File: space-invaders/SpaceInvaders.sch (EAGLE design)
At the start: 26 parts, among them J2_J4 TM4C123GXL, J3_J1 TM4C123GXL, J5 Nokia 5110, J6 Nokia 5110, U1 5V Voltage Regulator

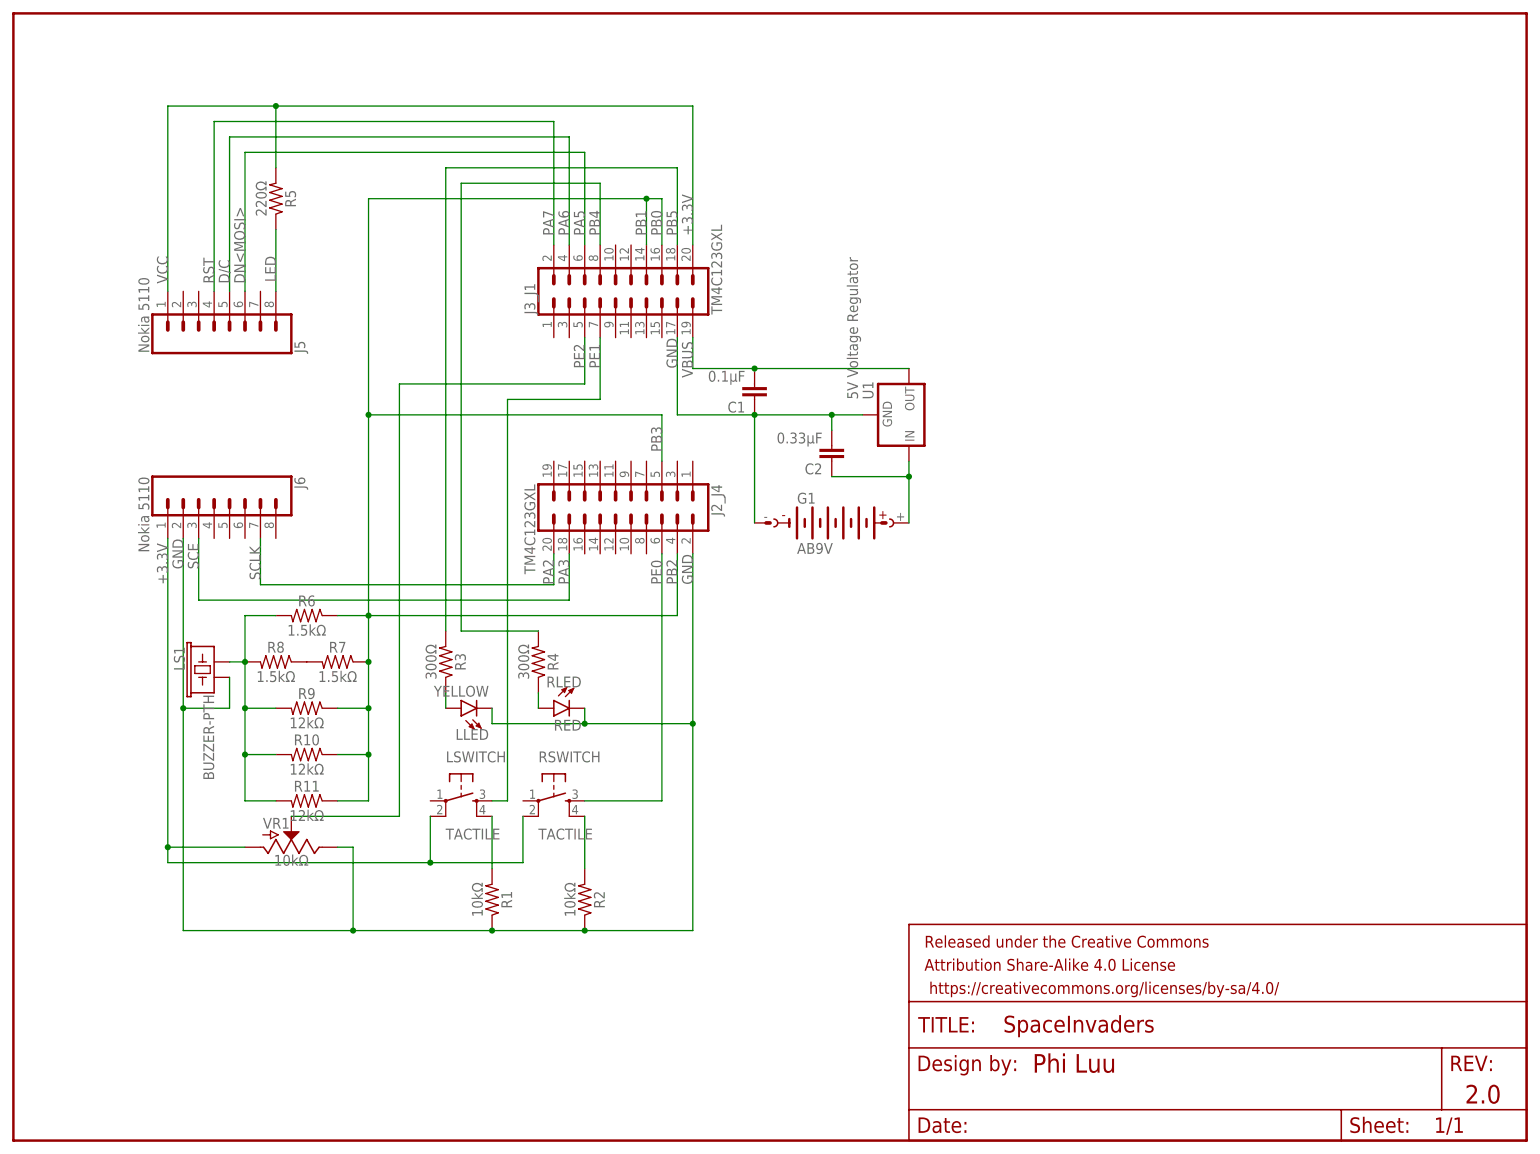
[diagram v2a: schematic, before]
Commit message: Setup SpaceInvaders regular manufacturing
Default EAGLE Design Rule Check (DRC). Double sided.
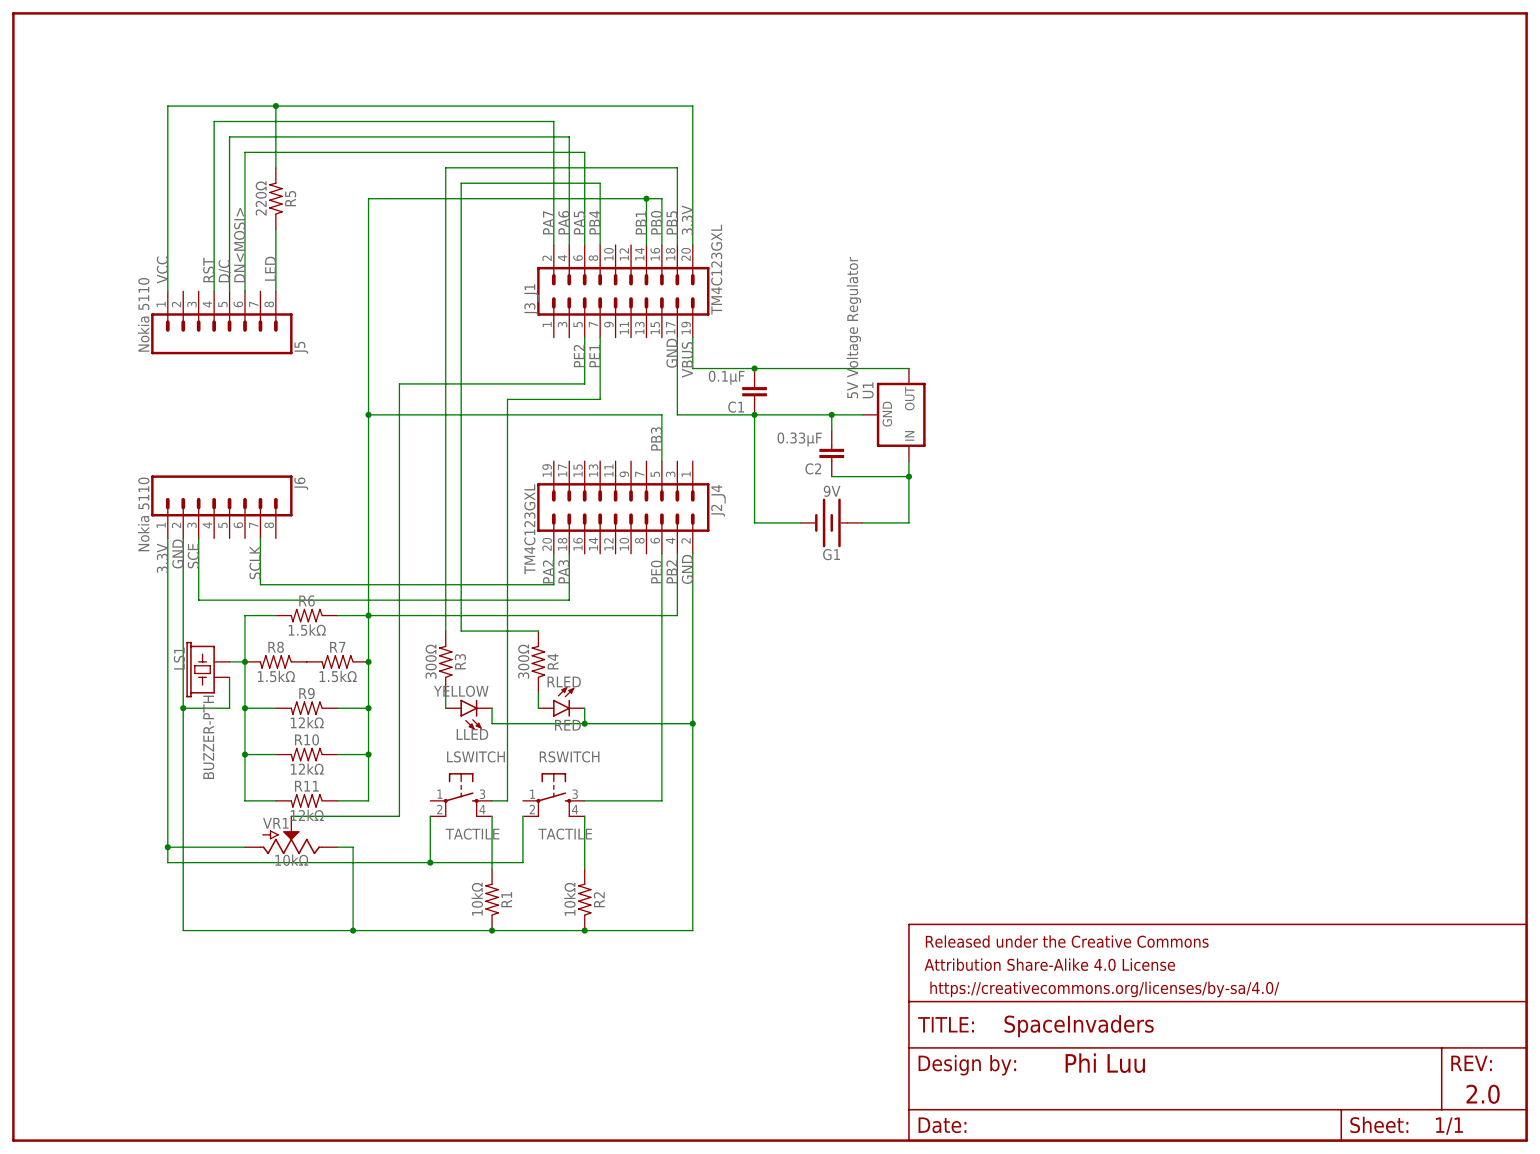
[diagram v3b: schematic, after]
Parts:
- G1: value AB9V -> 9V; device battery:AB9V -> SparkFun-Batteries:BATTERY-9V
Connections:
- net +3.3V renamed 3.3V
- net N$12 renamed LSWITCH_GND
- net N$14 renamed RSWITCH_GND
- net N$17 renamed RLED
- net N$19 renamed LLED
- net N$23 renamed DAC_OUT
- net N$24 renamed 9V
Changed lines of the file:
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@@
 <part name="C2" library="SparkFun-Capacitors" deviceset="0.1UF" device="-KIT-EZ-50V-20%" value="0.33μF"/>
 <part name="U1" library="SparkFun-IC-Power" deviceset="V_REG_78XX" device="-TO-220" value="5V Voltage Regulator"/>
-<part name="G1" library="battery" deviceset="AB9V" device=""/>
+<part name="G1" library="SparkFun-Batteries" deviceset="BATTERY" device="-9V" value="9V"/>
 <part name="FRAME1" library="SparkFun-Aesthetics" deviceset="FRAME-LETTER" device=""/>
 </parts>
@@
 <sheet>
 <plain>
-<text x="167.64" y="12.7" size="3.048" layer="94" font="vector" align="center-left">Phi Luu</text>
+<text x="172.72" y="12.7" size="3.048" layer="94" font="vector" align="center-left">Phi Luu</text>
 <text x="238.76" y="7.62" size="3.048" layer="94" font="vector" align="center-left">2.0</text>
 <text x="106.68" y="148.844" size="1.778" layer="96" font="vector" rot="R90">PB0</text>
@@
 <instance part="C2" gate="G$1" x="134.62" y="114.3" rot="R180"/>
 <instance part="U1" gate="G$1" x="147.32" y="119.38" rot="MR90"/>
-<instance part="G1" gate="G$1" x="134.62" y="101.6"/>
+<instance part="G1" gate="G$1" x="134.62" y="101.6" rot="R180"/>
 <instance part="FRAME1" gate="G$1" x="0" y="0"/>
 <instance part="FRAME1" gate="V" x="147.32" y="0"/>
@@
 </segment>
 </net>
-<net name="N$12" class="0">
+<net name="LSWITCH_GND" class="0">
 <segment>
 <pinref part="LSWITCH" gate="S" pin="4"/>
@@
 </segment>
 </net>
-<net name="N$14" class="0">
+<net name="RSWITCH_GND" class="0">
 <segment>
 <pinref part="RSWITCH" gate="S" pin="4"/>
@@
 </segment>
 </net>
-<net name="N$17" class="0">
+<net name="RLED" class="0">
 <segment>
 <pinref part="R4" gate="G$1" pin="1"/>
@@
 </segment>
 </net>
-<net name="N$19" class="0">
+<net name="LLED" class="0">
 <segment>
 <pinref part="R3" gate="G$1" pin="1"/>
@@
 </segment>
 </net>
-<net name="N$23" class="0">
+<net name="DAC_OUT" class="0">
 <segment>
 <pinref part="R6" gate="G$1" pin="2"/>
@@
 </segment>
 </net>
-<net name="N$24" class="0">
-<segment>
-<pinref part="G1" gate="G$1" pin="+"/>
+<net name="9V" class="0">
+<segment>
 <pinref part="U1" gate="G$1" pin="IN"/>
-<wire x1="147.32" y1="101.6" x2="147.32" y2="109.22" width="0.1524" layer="91"/>
 <pinref part="C2" gate="G$1" pin="1"/>
 <wire x1="147.32" y1="109.22" x2="147.32" y2="111.76" width="0.1524" layer="91"/>
 <wire x1="134.62" y1="109.22" x2="147.32" y2="109.22" width="0.1524" layer="91"/>
+<pinref part="G1" gate="G$1" pin="+"/>
+<wire x1="139.7" y1="101.6" x2="147.32" y2="101.6" width="0.1524" layer="91"/>
+<wire x1="147.32" y1="101.6" x2="147.32" y2="109.22" width="0.1524" layer="91"/>
 <junction x="147.32" y="109.22"/>
 </segment>
@@
 <wire x1="109.22" y1="119.38" x2="121.92" y2="119.38" width="0.1524" layer="91"/>
 <junction x="121.92" y="119.38"/>
-<pinref part="G1" gate="G$1" pin="-"/>
-<wire x1="121.92" y1="119.38" x2="121.92" y2="101.6" width="0.1524" layer="91"/>
 <pinref part="C2" gate="G$1" pin="2"/>
 <wire x1="134.62" y1="116.84" x2="134.62" y2="119.38" width="0.1524" layer="91"/>
 <junction x="134.62" y="119.38"/>
 <label x="109.22" y="127" size="1.778" layer="95" font="vector" rot="R90"/>
+<pinref part="G1" gate="G$1" pin="-"/>
+<wire x1="129.54" y1="101.6" x2="121.92" y2="101.6" width="0.1524" layer="91"/>
+<wire x1="121.92" y1="101.6" x2="121.92" y2="119.38" width="0.1524" layer="91"/>
 </segment>
 <segment>
@@
 </segment>
 </net>
-<net name="+3.3V" class="0">
+<net name="LED" class="0">
+<segment>
+<pinref part="R5" gate="G$1" pin="1"/>
+<pinref part="J5" gate="G$1" pin="8"/>
+<wire x1="43.18" y1="149.86" x2="43.18" y2="139.7" width="0.1524" layer="91"/>
+<label x="43.18" y="141.224" size="1.778" layer="95" font="vector" rot="R90"/>
+</segment>
+</net>
+<net name="PA3" class="0">
+<segment>
+<pinref part="J6" gate="G$1" pin="3"/>
+<wire x1="30.48" y1="99.06" x2="30.48" y2="88.9" width="0.1524" layer="91"/>
+<pinref part="J2_J4" gate="G$1" pin="18"/>
+<wire x1="30.48" y1="88.9" x2="91.44" y2="88.9" width="0.1524" layer="91"/>
+<wire x1="91.44" y1="88.9" x2="91.44" y2="96.52" width="0.1524" layer="91"/>
+<label x="91.44" y="91.44" size="1.778" layer="95" font="vector" rot="R90"/>
+</segment>
+</net>
+<net name="3.3V" class="0">
 <segment>
 <pinref part="J3_J1" gate="G$1" pin="20"/>
@@
 <wire x1="68.58" y1="53.34" x2="68.58" y2="45.72" width="0.1524" layer="91"/>
 <junction x="68.58" y="45.72"/>
-<label x="25.4" y="91.44" size="1.778" layer="95" font="vector" rot="R90"/>
-</segment>
-</net>
-<net name="LED" class="0">
-<segment>
-<pinref part="R5" gate="G$1" pin="1"/>
-<pinref part="J5" gate="G$1" pin="8"/>
-<wire x1="43.18" y1="149.86" x2="43.18" y2="139.7" width="0.1524" layer="91"/>
-<label x="43.18" y="141.224" size="1.778" layer="95" font="vector" rot="R90"/>
-</segment>
-</net>
-<net name="PA3" class="0">
-<segment>
-<pinref part="J6" gate="G$1" pin="3"/>
-<wire x1="30.48" y1="99.06" x2="30.48" y2="88.9" width="0.1524" layer="91"/>
-<pinref part="J2_J4" gate="G$1" pin="18"/>
-<wire x1="30.48" y1="88.9" x2="91.44" y2="88.9" width="0.1524" layer="91"/>
-<wire x1="91.44" y1="88.9" x2="91.44" y2="96.52" width="0.1524" layer="91"/>
-<label x="91.44" y="91.44" size="1.778" layer="95" font="vector" rot="R90"/>
+<label x="25.4" y="93.218" size="1.778" layer="95" font="vector" rot="R90"/>
 </segment>
 </net>
@@
 </sheet>
 </sheets>
+<errors>
+</errors>
 </schematic>
 </drawing>

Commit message: Update board SpaceInvaders
Add names to empty pins
Naming convention
Change switch package
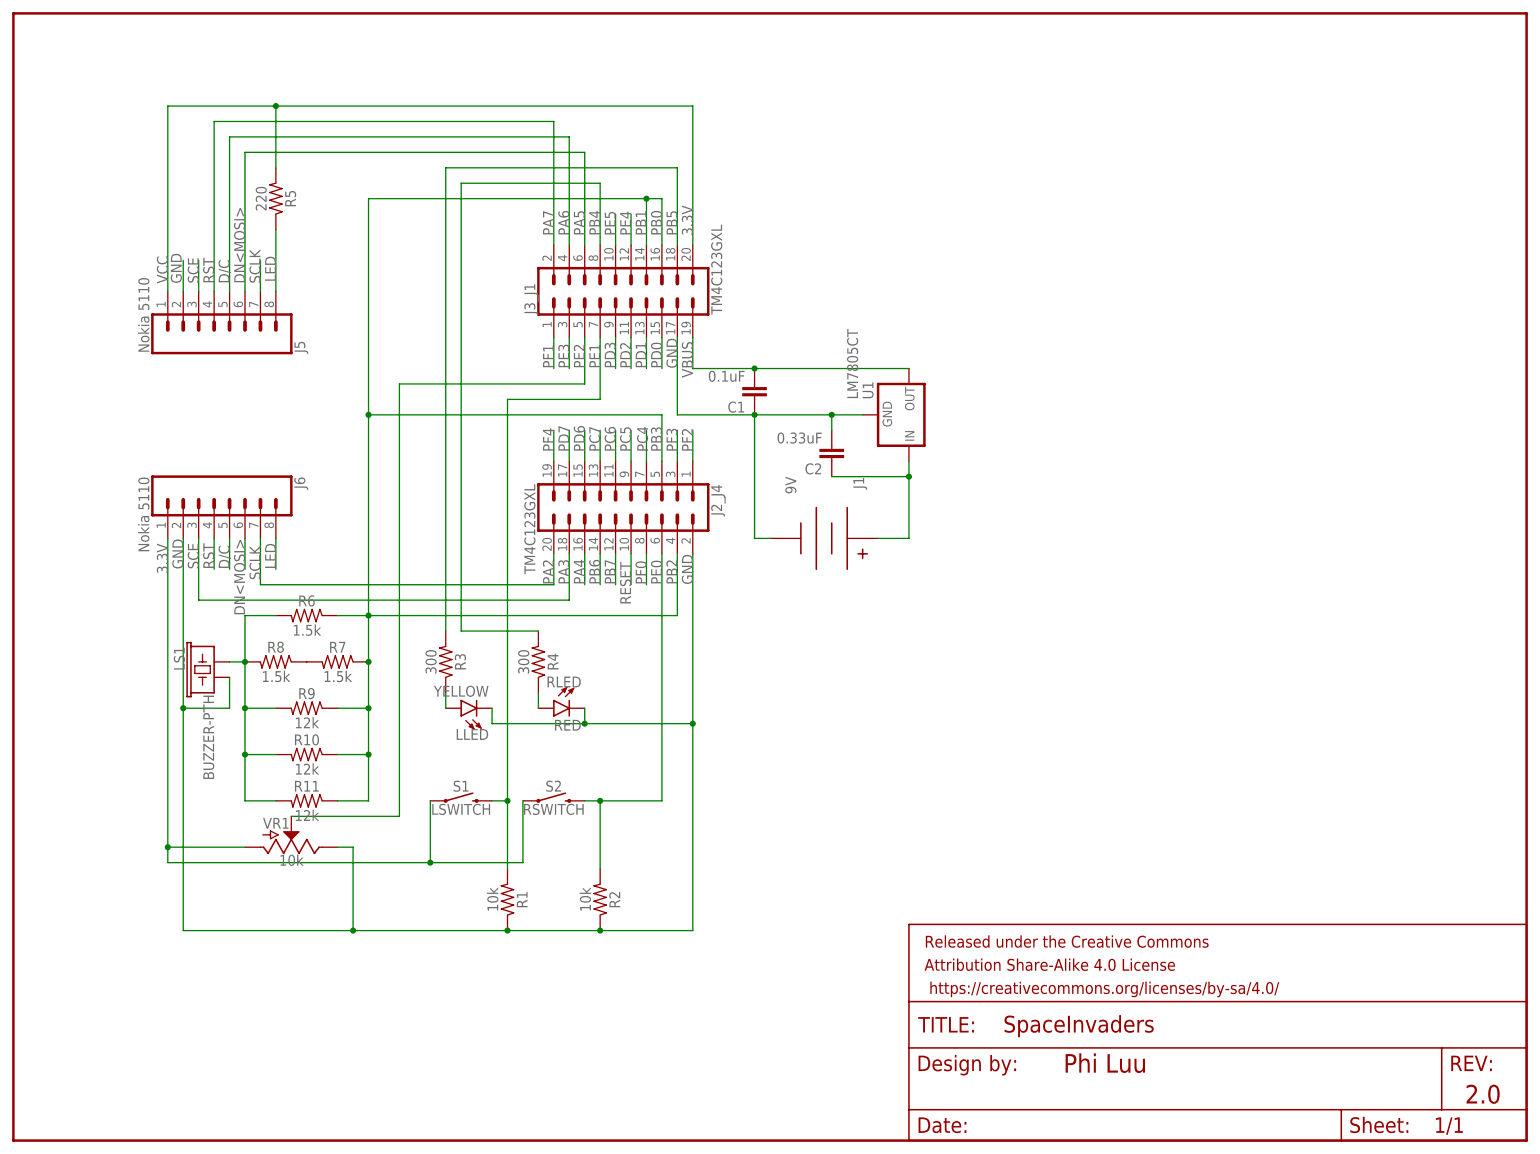
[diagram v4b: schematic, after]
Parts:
- removed G1: 9V, SparkFun-Batteries:BATTERY-9V
- removed LSWITCH, RSWITCH: TACTILE, SparkFun-Retired:TAC_SWITCHPTH
- added J1: 9V, SparkFun-Connectors:BC9VPC
- added S1: LSWITCH, SparkFun-Switches:MOMENTARY-SWITCH-SPST-PTH-6.0MM
- added S2: RSWITCH, SparkFun-Switches:MOMENTARY-SWITCH-SPST-PTH-6.0MM
- C1: value 0.1μF -> 0.1uF
- C2: value 0.33μF -> 0.33uF
- R1, R2, VR1: value 10kΩ -> 10k
- R10, R11, R9: value 12kΩ -> 12k
- R3, R4: value 300Ω -> 300
- R5: value 220Ω -> 220
- R6, R7, R8: value 1.5kΩ -> 1.5k
- U1: value 5V Voltage Regulator -> LM7805CT
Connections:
- removed net LSWITCH_GND: LSWITCH.4, R1.2
- removed net RSWITCH_GND: R2.2, RSWITCH.4
- new net D/C: J6.5
- new net DN<MOSI>: J6.6
- new net PA4: J2_J4.16
- new net PB6: J2_J4.14
- new net PB7: J2_J4.12
- new net PC4: J2_J4.7
- new net PC5: J2_J4.9
- new net PC6: J2_J4.11
- new net PC7: J2_J4.13
- new net PD0: J3_J1.15
- new net PD1: J3_J1.13
- new net PD2: J3_J1.11
- new net PD3: J3_J1.9
- new net PD6: J2_J4.15
- new net PD7: J2_J4.17
- new net PE3: J3_J1.3
- new net PE4: J3_J1.12
- new net PE5: J3_J1.10
- new net PF0: J2_J4.8
- new net PF1: J3_J1.1
- new net PF2: J2_J4.1
- new net PF3: J2_J4.3
- new net PF4: J2_J4.19
- new net RESET: J2_J4.10
- new net RST: J6.4
- new net SCE: J5.3
- new net SCLK: J5.7
- net 3.3V: now also S1.1, S2.1; no longer LSWITCH.2, RSWITCH.2
- net 9V: now also J1.V+; no longer G1.+
- net GND: now also J1.V-, J5.2; no longer G1.-
- net LED: now also J6.8
- net PE0: now also R2.2, S2.2; no longer RSWITCH.3
- net PE1: now also R1.2, S1.2; no longer LSWITCH.3
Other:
- moved on the sheet: R1, R2

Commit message: Follow naming convention - English letter only
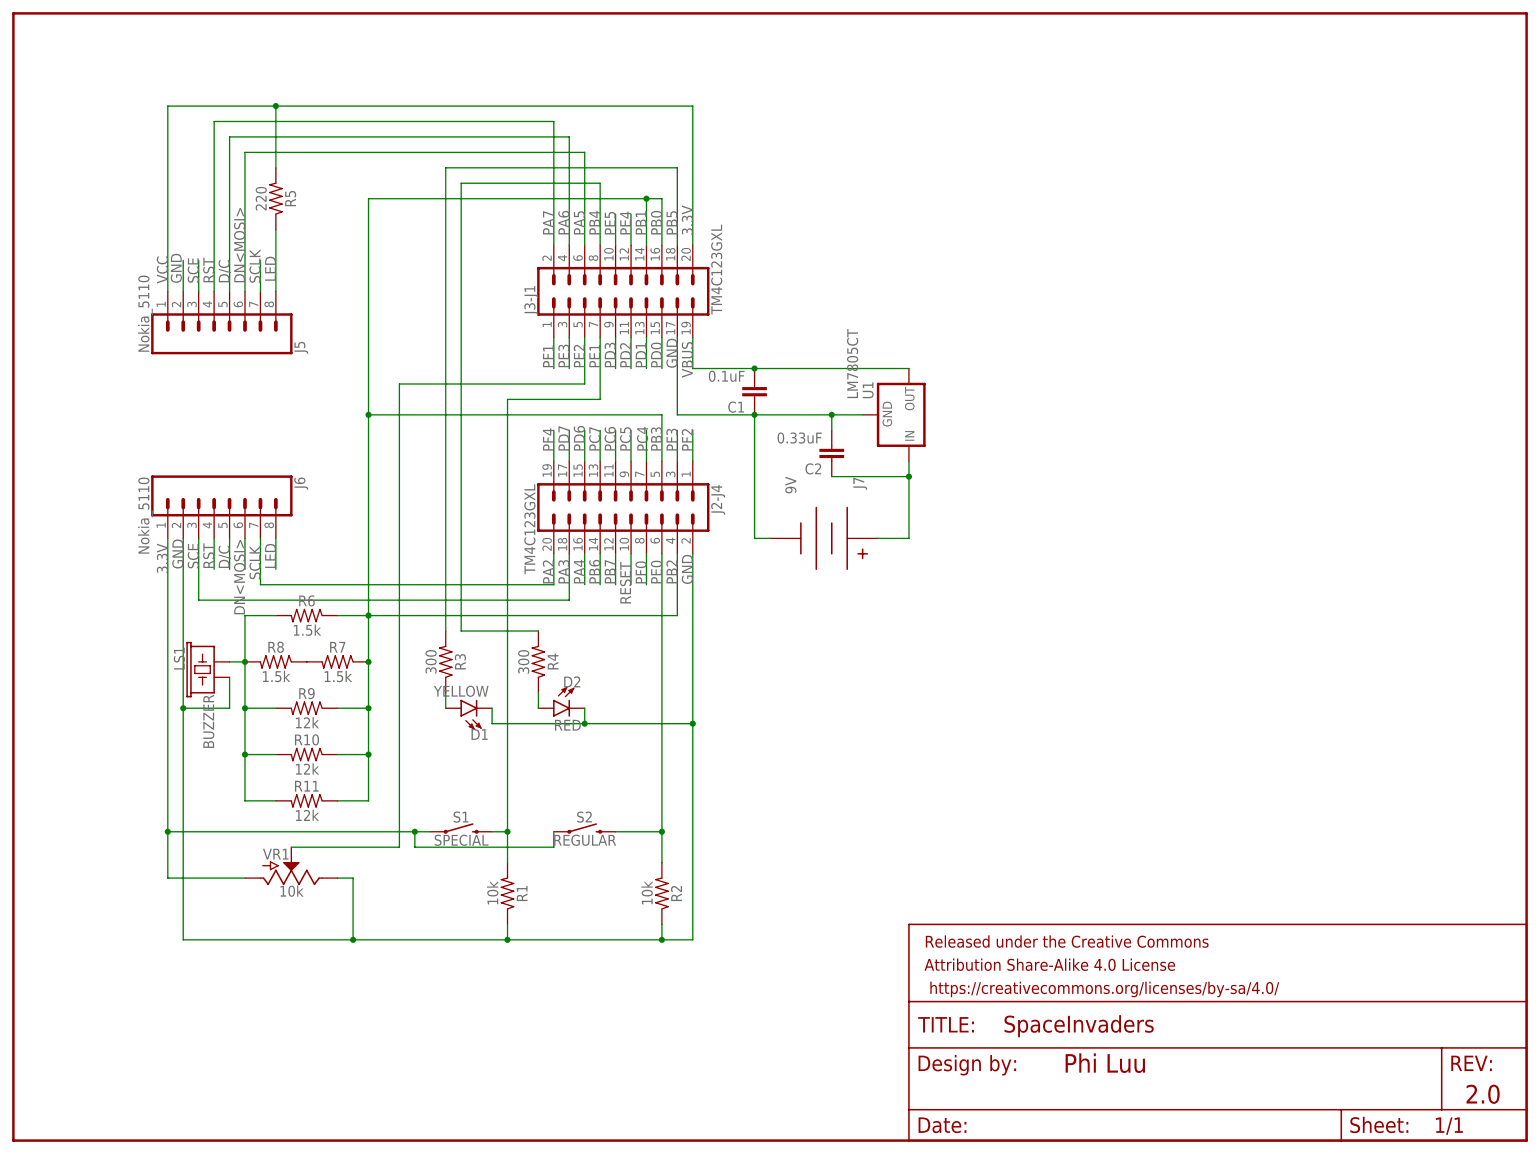
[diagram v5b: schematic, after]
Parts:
- J5, J6: value Nokia 5110 -> Nokia_5110
- LS1: value BUZZER-PTH -> BUZZER
- S1: value LSWITCH -> SPECIAL
- S2: value RSWITCH -> REGULAR
- renumbered J1 to J7, J2_J4 to J2-J4, J3_J1 to J3-J1, LLED to D1, RLED to D2
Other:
- moved on the sheet: R1, R2, S1, S2, VR1
